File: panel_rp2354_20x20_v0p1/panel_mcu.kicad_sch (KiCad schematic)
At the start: 32 parts, among them SW1 SW_Push, SW2 SW_Push, U1 APS6404L-3SQR, U2 RP2354B_80QFN, Y1 ABM8-272-T3

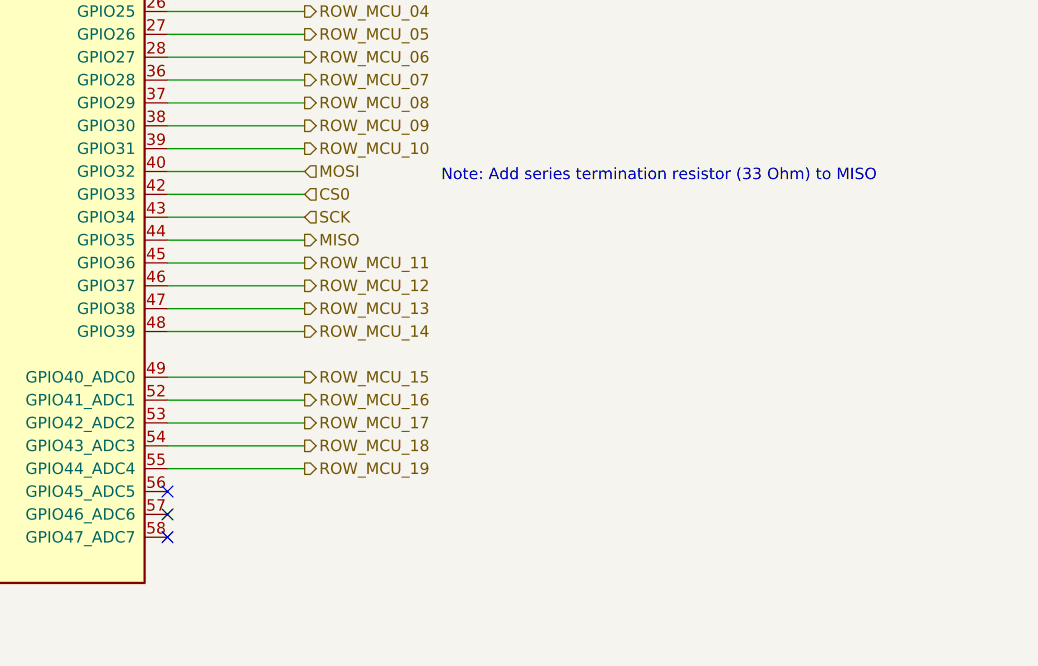
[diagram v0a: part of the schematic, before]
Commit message: Add MISO series resistor and connect EINT to MCU
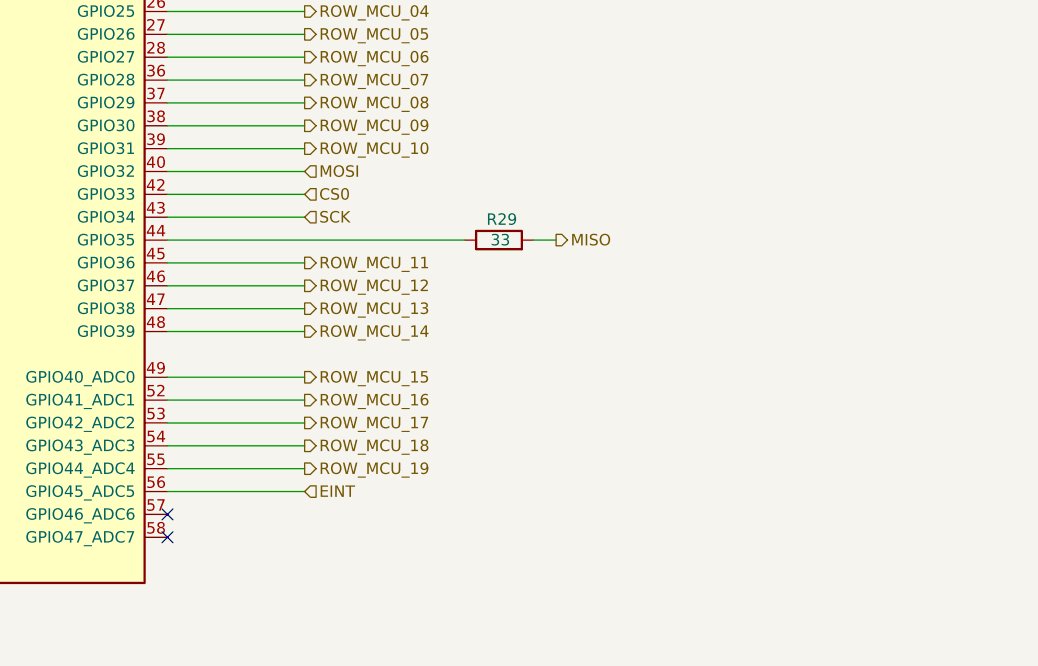
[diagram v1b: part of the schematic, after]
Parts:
- added R29: 33, panel_custom:R_0201_0603Metric, symbol Device:R
- C1, C10, C11, C12, C13, C14, C15, C16, C17, C18, C2, C3, C6, C9: footprint Capacitor_SMD:C_0201_0603Metric -> panel_custom:C_0201_0603Metric
- C4, C5: footprint RP2350_80QFN_minimal:C_0402_1005Metric_small_pads -> panel_custom:C_0402_1005Metric_small_pads
- C7, C8: footprint Capacitor_SMD:C_0402_1005Metric -> panel_custom:C_0402_1005Metric
- L1: footprint RP2350_80QFN_minimal:L_pol_2016 -> panel_custom:L_pol_2016
- R1, R2, R3, R4, R5, R6, R7, R8: footprint Resistor_SMD:R_0201_0603Metric -> panel_custom:R_0201_0603Metric
- U2: footprint RP2350_80QFN_minimal:RP2350-QFN-80-1EP_10x10_P0.4mm_EP3.4x3.4mm_ThermalVias -> panel_custom:RP2350-QFN-80-1EP_10x10_P0.4mm_EP3.4x3.4mm_ThermalVias
- Y1: footprint Crystal:Crystal_SMD_3225-4Pin_3.2x2.5mm -> panel_custom:Crystal_SMD_3225-4Pin_3.2x2.5mm; symbol Device:Crystal_GND24 -> panel_custom:Crystal_GND24
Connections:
- net MISO: now also R29.2; no longer U2.44 (GPIO35)
- net EINT: now reaches U2.56 (GPIO45_ADC5)
- new net: R29.1, U2.44 (GPIO35)
- no-connect marks 5 -> 4
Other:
- note removed: "Note: Add series termination resistor (33 Ohm) to MISO"
- company: (none) -> Janelia Research Campus
- title: (none) -> G6 Panel
